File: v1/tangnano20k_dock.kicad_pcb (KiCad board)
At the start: 2 copper layers, 136.5 x 73.7 mm, 77 parts, among them J1 Mini-DIN-6, J10 DB9_Male_MountingHoles, J11 DB9_Male_MountingHoles, J2 2x20 Pin Female, J3 Conn_01x03_Male, J4 Conn_01x20, J5 Conn_01x02, J6 RCA, J7 FCR684205T, J8 AudioJack3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

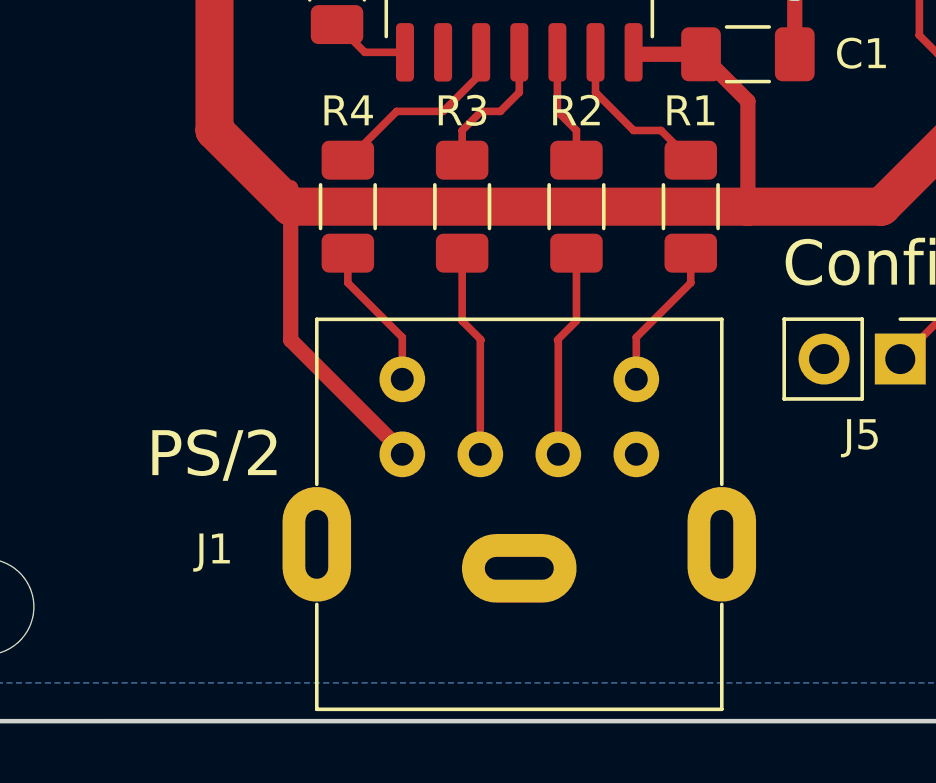
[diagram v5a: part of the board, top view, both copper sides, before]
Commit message: Corrected error in PS/2 footprint
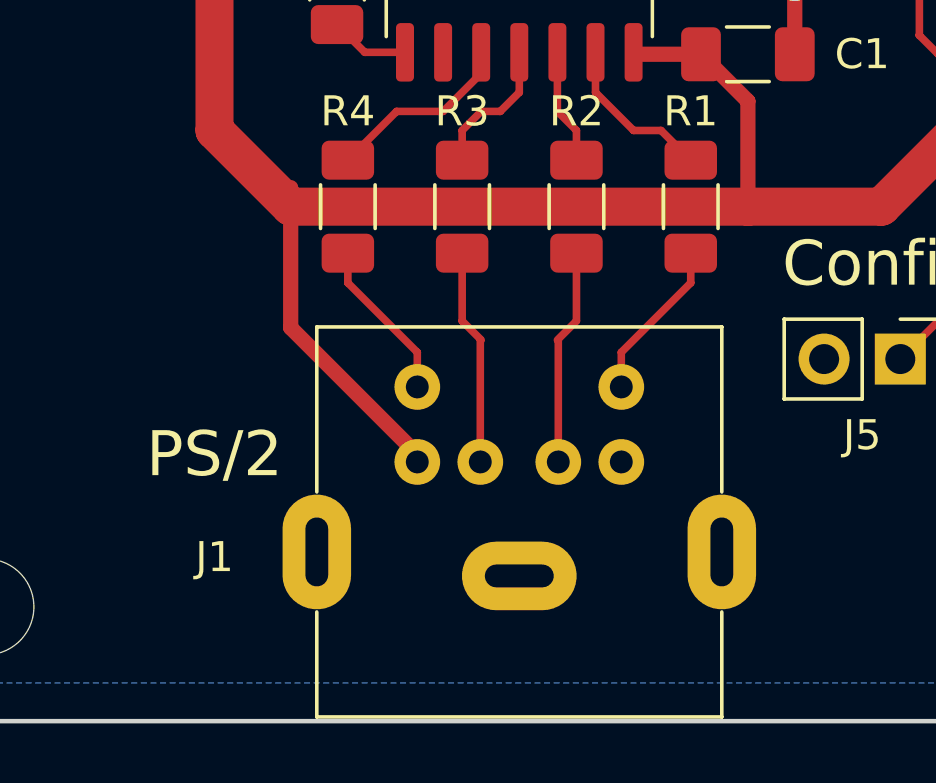
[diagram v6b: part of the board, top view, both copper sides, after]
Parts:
- moved J1 0.25 mm to (94.6, 114.5)
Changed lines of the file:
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@@
   )
   (footprint "TangNano20k:minidin6" (layer "F.Cu")
-    (at 94.615 114.295 180)
+    (at 94.615 114.549 180)
     (property "Sheetfile" "tangnano20k_dock.kicad_sch")
     (property "Sheetname" "")
@@
     )
     (fp_line (start -6.75 -8.5) (end 6.75 -8.5) (layer "F.SilkS") (width 0.12))
+    (fp_line (start -6.75 -8.5) (end -6.75 -5) (layer "F.SilkS") (width 0.12))
     (fp_line (start -6.75 -1) (end -6.75 4.5) (layer "F.SilkS") (width 0.12))
+    (fp_line (start 6.75 -8.5) (end 6.75 -5) (layer "F.SilkS") (width 0.12))
+    (fp_line (start 6.75 -1) (end 6.75 4.5) (layer "F.SilkS") (width 0.12))
     (fp_line (start 6.75 4.5) (end -6.75 4.5) (layer "F.SilkS") (width 0.12))
-    (fp_line (start -6.75 -8.5) (end -6.75 -5) (layer "F.SilkS") (width 0.12))
-    (fp_line (start 6.75 -1) (end 6.75 4.5) (layer "F.SilkS") (width 0.12))
-    (fp_line (start 6.75 -8.5) (end 6.75 -5) (layer "F.SilkS") (width 0.12))
-    (fp_line (start 6.85 4.6) (end -6.85 4.6) (layer "F.CrtYd") (width 0.12))
     (fp_line (start -6.85 4.6) (end -6.85 -8.6) (layer "F.CrtYd") (width 0.12))
     (fp_line (start -6.85 -8.6) (end 6.85 -8.6) (layer "F.CrtYd") (width 0.12))
     (fp_line (start 6.85 -8.6) (end 6.85 4.6) (layer "F.CrtYd") (width 0.12))
+    (fp_line (start 6.85 4.6) (end -6.85 4.6) (layer "F.CrtYd") (width 0.12))
+    (pad "" thru_hole oval (at 6.75 -3 180) (size 2.286 3.824) (drill oval 0.762 2.3) (layers *.Cu *.Mask))
     (pad "" thru_hole oval (at 0 -3.8 90) (size 2.286 3.824) (drill oval 0.762 2.3) (layers *.Cu *.Mask))
     (pad "" thru_hole oval (at -6.75 -3 180) (size 2.286 3.824) (drill oval 0.762 2.3) (layers *.Cu *.Mask))
-    (pad "" thru_hole oval (at 6.75 -3 180) (size 2.286 3.824) (drill oval 0.762 2.3) (layers *.Cu *.Mask))
     (pad "1" thru_hole circle (at -1.3 0 180) (size 1.524 1.524) (drill 0.762) (layers *.Cu *.Mask)
       (net 9 "Net-(J1-Pad1)") (pintype "passive"))
     (pad "2" thru_hole circle (at 1.3 0 180) (size 1.524 1.524) (drill 0.762) (layers *.Cu *.Mask)
       (net 10 "Net-(J1-Pad2)") (pintype "passive"))
-    (pad "3" thru_hole circle (at -3.9 0 180) (size 1.524 1.524) (drill 0.762) (layers *.Cu *.Mask)
+    (pad "3" thru_hole circle (at -3.4 0 180) (size 1.524 1.524) (drill 0.762) (layers *.Cu *.Mask)
       (net 1 "GND") (pintype "passive"))
-    (pad "4" thru_hole circle (at 3.9 0 180) (size 1.524 1.524) (drill 0.762) (layers *.Cu *.Mask)
+    (pad "4" thru_hole circle (at 3.4 0 180) (size 1.524 1.524) (drill 0.762) (layers *.Cu *.Mask)
       (net 2 "+5V") (pintype "passive"))
-    (pad "5" thru_hole circle (at -3.9 2.5 180) (size 1.524 1.524) (drill 0.762) (layers *.Cu *.Mask)
+    (pad "5" thru_hole circle (at -3.4 2.5 180) (size 1.524 1.524) (drill 0.762) (layers *.Cu *.Mask)
       (net 11 "Net-(J1-Pad5)") (pintype "passive"))
-    (pad "6" thru_hole circle (at 3.9 2.5 180) (size 1.524 1.524) (drill 0.762) (layers *.Cu *.Mask)
+    (pad "6" thru_hole circle (at 3.4 2.5 180) (size 1.524 1.524) (drill 0.762) (layers *.Cu *.Mask)
       (net 12 "Net-(J1-Pad6)") (pintype "passive"))
   )
@@
   (segment (start 143.51 115.57) (end 145.415 117.475) (width 1.27) (layer "F.Cu") (net 2))
   (segment (start 106.685 106.04) (end 102.235 106.04) (width 1.27) (layer "F.Cu") (net 2))
-  (segment (start 86.995 110.485) (end 86.995 105.405) (width 0.508) (layer "F.Cu") (net 2))
   (segment (start 91.44 87.625) (end 91.44 83.185) (width 0.508) (layer "F.Cu") (net 2))
   (segment (start 201.295 114.935) (end 201.295 55.24) (width 1.27) (layer "F.Cu") (net 2))
@@
   (segment (start 91.44 83.185) (end 91.44 81.91) (width 0.254) (layer "F.Cu") (net 2))
   (segment (start 165.735 107.95) (end 160.655 113.03) (width 0.508) (layer "F.Cu") (net 2))
+  (segment (start 91.215 114.295) (end 86.995 110.075) (width 0.508) (layer "F.Cu") (net 2))
   (segment (start 143.51 112.7125) (end 143.51 115.57) (width 1.27) (layer "F.Cu") (net 2))
   (segment (start 136.8375 106.04) (end 143.51 112.7125) (width 1.27) (layer "F.Cu") (net 2))
   (segment (start 102.235 106.04) (end 102.235 102.5225) (width 0.508) (layer "F.Cu") (net 2))
   (segment (start 183.225 117.185) (end 183.515 117.475) (width 0.508) (layer "F.Cu") (net 2))
+  (segment (start 86.995 110.075) (end 86.995 105.405) (width 0.508) (layer "F.Cu") (net 2))
   (segment (start 100.6725 100.96) (end 98.49 100.96) (width 0.508) (layer "F.Cu") (net 2))
   (segment (start 201.295 55.24) (end 200.66 54.605) (width 1.27) (layer "F.Cu") (net 2))
-  (segment (start 90.715 114.205) (end 86.995 110.485) (width 0.508) (layer "F.Cu") (net 2))
   (segment (start 196.215 59.05) (end 196.215 56.51) (width 1.27) (layer "F.Cu") (net 2))
   (segment (start 145.415 117.475) (end 150.495 117.475) (width 1.27) (layer "F.Cu") (net 2))
@@
   (segment (start 82.55 69.5025) (end 84.1125 67.94) (width 0.254) (layer "F.Cu") (net 8))
   (segment (start 87.8225 63.7925) (end 90.14 61.475) (width 0.254) (layer "F.Cu") (net 8))
+  (segment (start 95.915 114.549) (end 95.915 110.515) (width 0.254) (layer "F.Cu") (net 9))
   (segment (start 96.52 107.59) (end 96.52 109.85) (width 0.254) (layer "F.Cu") (net 9))
   (segment (start 96.52 109.85) (end 95.885 110.485) (width 0.254) (layer "F.Cu") (net 9))
-  (segment (start 95.915 114.295) (end 95.915 110.515) (width 0.254) (layer "F.Cu") (net 9))
   (segment (start 92.71 107.59) (end 92.71 109.85) (width 0.254) (layer "F.Cu") (net 10))
-  (segment (start 93.315 114.295) (end 93.315 110.485) (width 0.254) (layer "F.Cu") (net 10))
+  (segment (start 93.315 114.549) (end 93.315 110.485) (width 0.254) (layer "F.Cu") (net 10))
   (segment (start 92.71 109.85) (end 93.345 110.485) (width 0.254) (layer "F.Cu") (net 10))
-  (segment (start 98.515 111.795) (end 98.515 110.395) (width 0.254) (layer "F.Cu") (net 11))
+  (segment (start 98.015 112.049) (end 98.015 110.895) (width 0.254) (layer "F.Cu") (net 11))
   (segment (start 100.33 108.58) (end 100.33 107.59) (width 0.254) (layer "F.Cu") (net 11))
-  (segment (start 98.515 110.395) (end 100.33 108.58) (width 0.254) (layer "F.Cu") (net 11))
+  (segment (start 98.015 110.895) (end 100.33 108.58) (width 0.254) (layer "F.Cu") (net 11))
   (segment (start 88.9 108.58) (end 88.9 107.59) (width 0.254) (layer "F.Cu") (net 12))
-  (segment (start 90.715 111.795) (end 90.715 110.395) (width 0.254) (layer "F.Cu") (net 12))
-  (segment (start 90.715 110.395) (end 88.9 108.58) (width 0.254) (layer "F.Cu") (net 12))
+  (segment (start 91.215 110.895) (end 88.9 108.58) (width 0.254) (layer "F.Cu") (net 12))
+  (segment (start 91.215 112.049) (end 91.215 110.895) (width 0.254) (layer "F.Cu") (net 12))
   (segment (start 133.345 97.155) (end 133.35 97.15) (width 0.254) (layer "F.Cu") (net 13))
   (segment (start 107.315 111.12) (end 110.49 107.945) (width 0.254) (layer "F.Cu") (net 13))

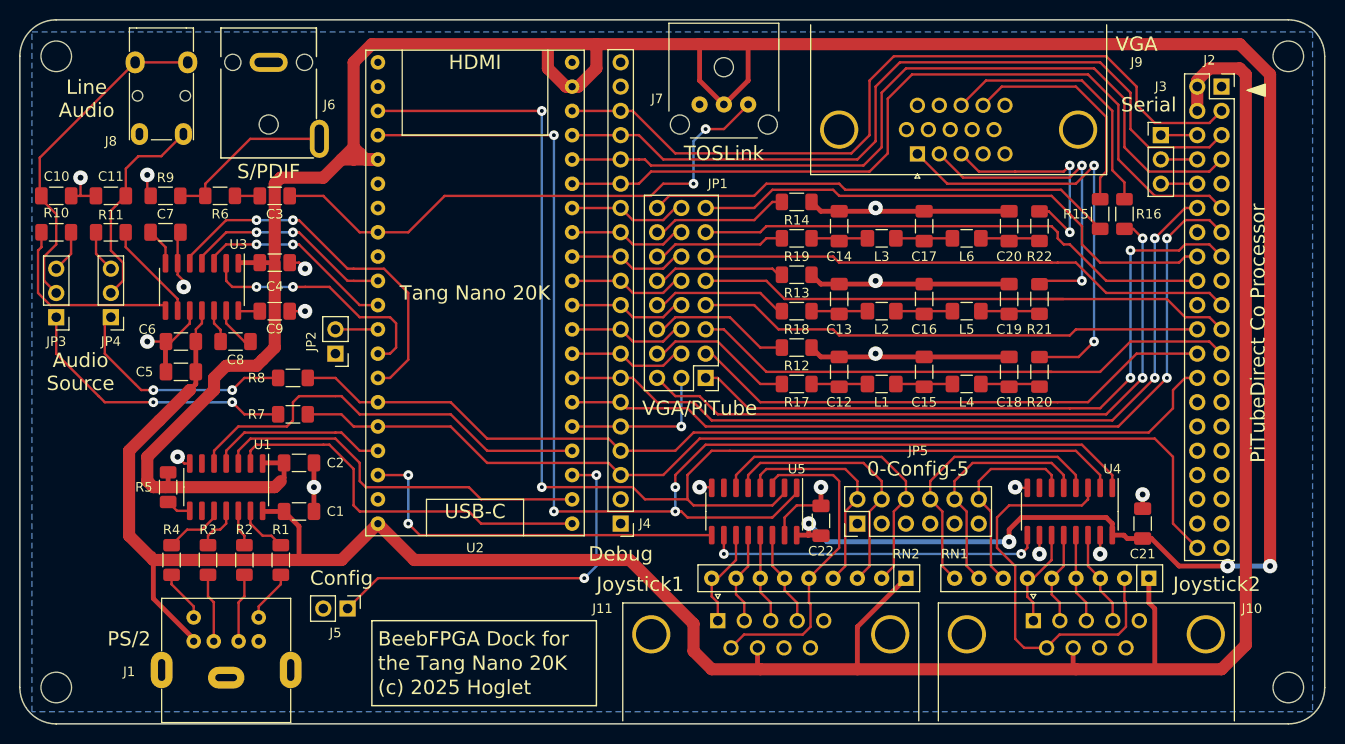
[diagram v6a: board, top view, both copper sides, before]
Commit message: Silk-screen and swap PWM L/R labels
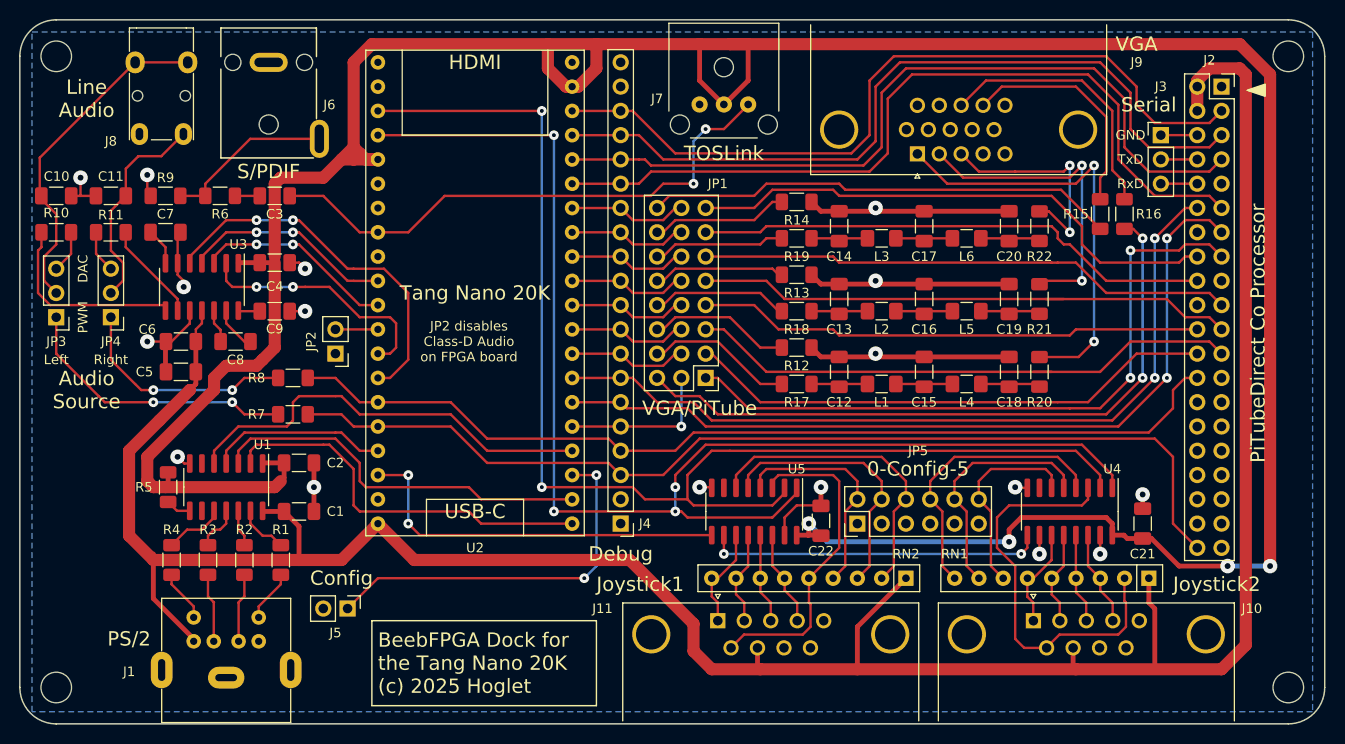
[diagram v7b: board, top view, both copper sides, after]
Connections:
- net Net-(C10-Pad2) renamed /LEFT
- net Net-(C11-Pad2) renamed /RIGHT
- J2 pad 26: /PWM_L -> /PWM_R
- J2 pad 40: /PWM_R -> /PWM_L
- J4 pad 3: /PWM_R -> /PWM_L
- J4 pad 4: /PWM_L -> /PWM_R
- JP3 pad 1: /RC_AUDIO_R -> /RC_AUDIO_L
- JP4 pad 1: /RC_AUDIO_L -> /RC_AUDIO_R
- R7 pad 1: /RC_AUDIO_R -> /RC_AUDIO_L
- R7 pad 2: /PWM_R -> /PWM_L
- R8 pad 1: /RC_AUDIO_L -> /RC_AUDIO_R
- R8 pad 2: /PWM_L -> /PWM_R
- U2 pad 35: /PWM_L -> /PWM_R
- U2 pad 36: /PWM_R -> /PWM_L
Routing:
- net /RC_AUDIO_L: track 23.4 -> 29.7 mm
- net /RC_AUDIO_R: track 29.7 -> 23.8 mm
- net /PWM_R: track 106.1 -> 100.5 mm
- net /PWM_L: track 100.5 -> 106.1 mm
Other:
- board text added: "BeebFPGA Dock for the Tang Nano 20K (c) 2025 Hoglet"
- board text added: "DAC"
- board text added: "GND"
- board text added: "JP2 disables Class-D Audio on FPGA board"
- board text added: "Left"
- board text added: "PWM"
- board text added: "Right"
- board text added: "RxD"
- board text added: "TxD"

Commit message: Added jumpers for Pi and Joystick power
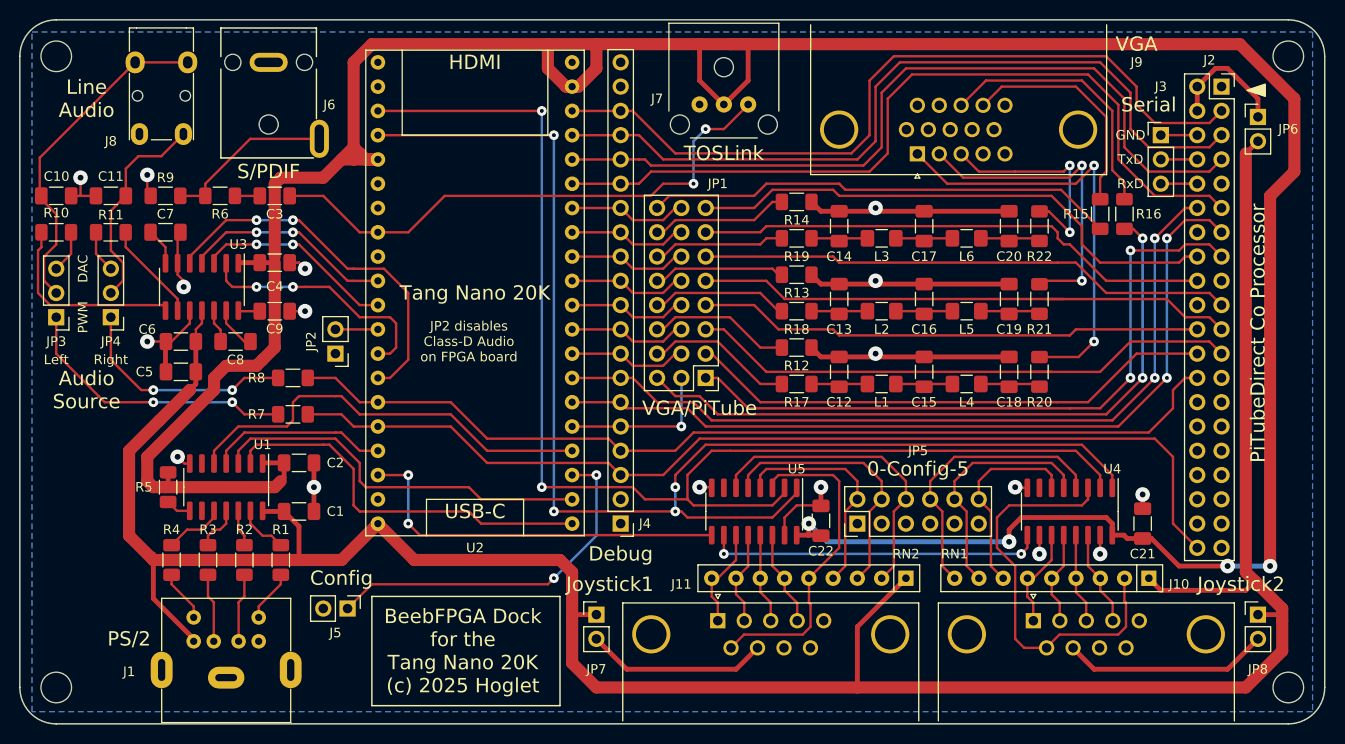
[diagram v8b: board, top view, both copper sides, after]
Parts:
- added JP6: Jumper_2_Bridged, Connector_PinHeader_2.54mm:PinHeader_1x02_P2.54mm_Vertical, F.Cu at (202.6, 59.7)
- added JP7: Jumper_2_Open, Connector_PinHeader_2.54mm:PinHeader_1x02_P2.54mm_Vertical, F.Cu at (133.3, 111.8)
- added JP8: Jumper_2_Open, Connector_PinHeader_2.54mm:PinHeader_1x02_P2.54mm_Vertical, F.Cu at (202.6, 111.8)
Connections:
- J10 pad 7: +5V -> Net-(J10-Pad7)
- J11 pad 7: +5V -> Net-(J11-Pad7)
- J2 pad 2: +5V -> Net-(J2-Pad2)
- J2 pad 4: +5V -> Net-(J2-Pad2)
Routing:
- net Net-(J10-Pad7): track 0.00 -> 21.6 mm
- net Net-(J11-Pad7): track 0.00 -> 19.1 mm
- net Net-(J2-Pad2): track 0.00 -> 12.9 mm
- net +3.3V: track 323.8 -> 325.9 mm
- net /KBD_CONFIG_MODIFIER: track 39.9 -> 38.1 mm
